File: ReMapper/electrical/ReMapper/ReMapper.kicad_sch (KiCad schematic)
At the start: 2 parts, among them U1 ESP32-S3-WROOM-1-N8R8, U2 SC0914_13_

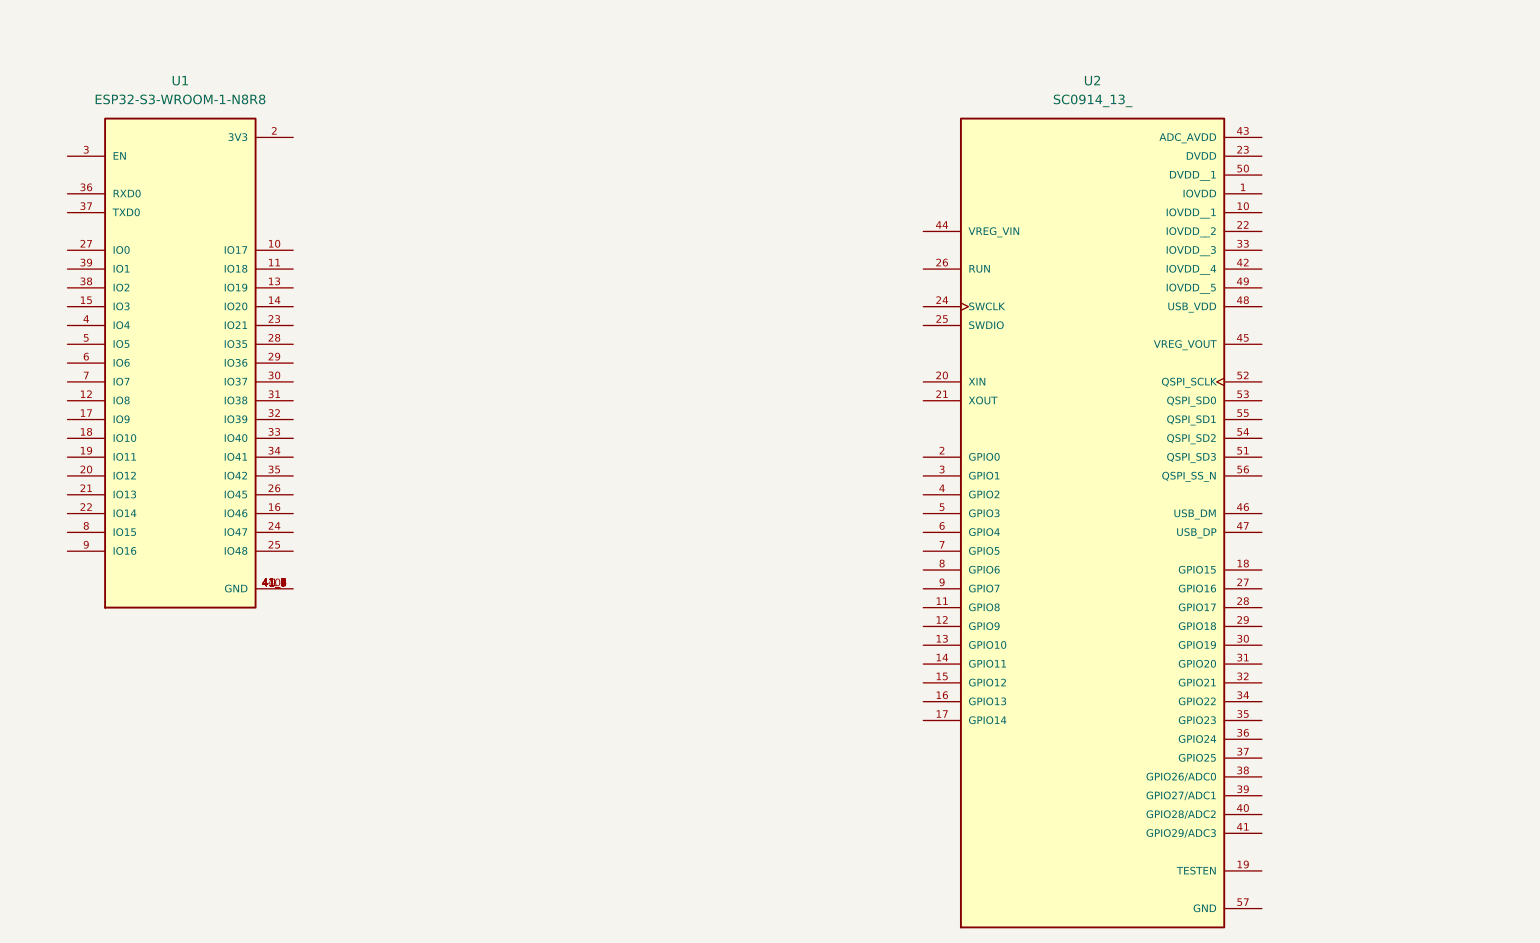
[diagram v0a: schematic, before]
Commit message: started working real schamtic
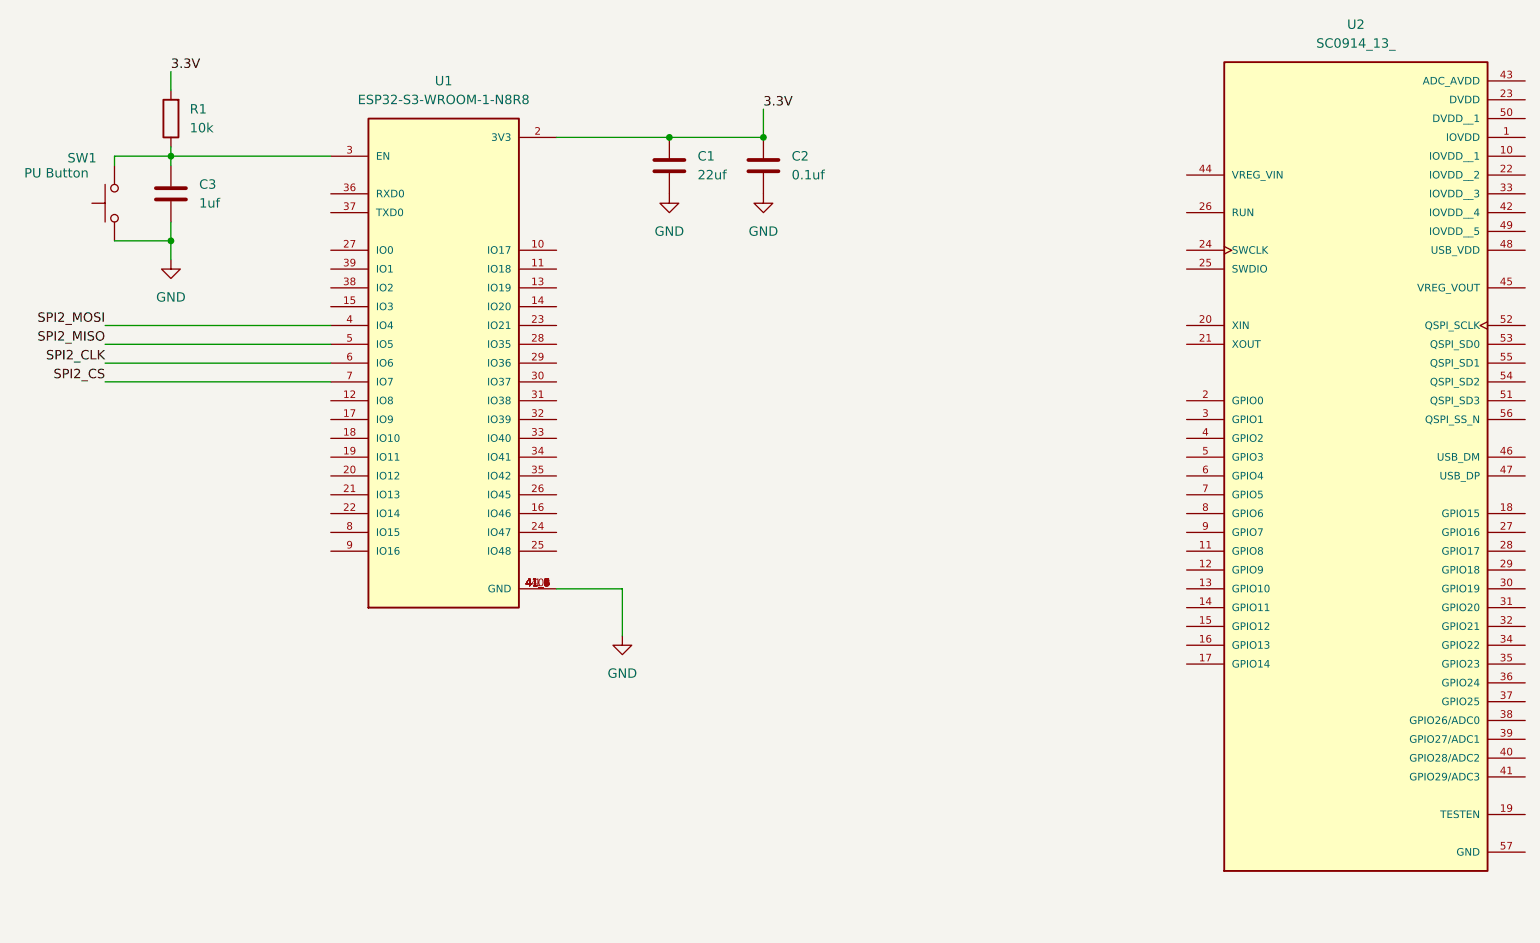
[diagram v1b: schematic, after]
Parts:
- added C1: 22uf, symbol Device:C
- added C2: 0.1uf, symbol Device:C
- added C3: 1uf, symbol Device:C
- added R1: 10k, symbol Device:R
- added SW1: PU Button, symbol Switch:SW_Push
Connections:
- net GND: now reaches U1.1 (GND), U1.40 (GND), U1.41_1 (GND), U1.41_2 (GND), U1.41_3 (GND), U1.41_4 (GND), U1.41_5 (GND), U1.41_6 (GND), U1.41_7 (GND), U1.41_8 (GND), U1.41_9 (GND)
- net GND: now also C1.2, C2.2, C3.2, SW1.1
- net 3.3V: now reaches U1.2 (3V3)
- net 3.3V: now also C1.1, C2.1, R1.2
- net at U1.3 (EN): now also C3.1, R1.1, SW1.2
- net SPI2_MOSI: now reaches U1.4 (IO4)
- net SPI2_MISO: now reaches U1.5 (IO5)
- net SPI2_CLK: now reaches U1.6 (IO6)
- net SPI2_CS: now reaches U1.7 (IO7)
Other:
- moved on the sheet: U1, U2

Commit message: more work on schematic
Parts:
- added C4: 2.2uf, symbol Device:C
- added C5: 100nf, symbol Device:C
- added C6, C7, C8: 47uF, symbol Device:C
- added D1: D_Schottky, symbol Device:D_Schottky
- added D2, D3, D4, D5: ESD, Diode_SMD:D_SOD-523, symbol Diode:ESD9B5.0ST5G
- added J1: QSPI_Debug, Connector_PinHeader_1.00mm:PinHeader_1x08_P1.00mm_Vertical, symbol Connector:Conn_01x08_Pin
- added J2: USB_IN, footprints:USBA_Female, symbol Connector:USB_A
- added J3: USB__IN_Debug, Connector_PinHeader_1.00mm:PinHeader_1x02_P1.00mm_Vertical, symbol Connector:Conn_01x02_Pin
- added J4: ESP_UART0, Connector_PinHeader_1.00mm:PinHeader_1x04_P1.00mm_Vertical, symbol Connector:Conn_01x04_Pin
- added J5: USB_OUT, footprints:USBA_Female, symbol Connector:USB_A
- added JP1: PFM Mode, Jumper:SolderJumper-2_P1.3mm_Open_Pad1.0x1.5mm, symbol Jumper:SolderJumper_2_Open
- added JP2, JP3: GND_SHIELD, Jumper:SolderJumper-2_P1.3mm_Open_Pad1.0x1.5mm, symbol Jumper:SolderJumper_2_Open
- added L1: 2.2uH, symbol Device:L
- added R2: 100k, symbol Device:R
- added U3: W25Q128JVE, Package_SON:WSON-8-1EP_8x6mm_P1.27mm_EP3.4x4.3mm, symbol Memory_Flash:W25Q128JVE
- added U4: RT6150B-33GQW, footprints:RT6150B-33GQW, symbol RT6150B-33GQW:RT6150B-33GQW
- U2: value SC0914_13_ -> RP2040
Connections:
- net 3.3V: now also C4.1, C5.1, C6.1, J1.7 (Pin_7), J4.1 (Pin_1), U3.8 (VCC), U4.1 (VOUT), U4.10 (FB)
- net GND: now also C4.2, C5.2, C6.2, C7.2, C8.2, D2.2 (A2), D3.1 (A1), D4.2 (A2), D5.1 (A1), J1.8 (Pin_8), J2.4 (GND), J4.4 (Pin_4), J5.4 (GND), JP2.2 (B), JP3.2 (B), R2.2, U3.4 (GND), U4.3 (GND), U4.9 (GND__1)
- net QSPI_CS_esp: now reaches U1.10 (IO17)
- net QSPI_CS_esp: now also J1.1 (Pin_1), U3.1 (~{CS})
- net USB_OUT_D+: now reaches U1.13 (IO19)
- net USB_OUT_D+: now also D2.1 (A1), J5.3 (D+)
- net USB_OUT_D-: now reaches U1.14 (IO20)
- net USB_OUT_D-: now also D3.2 (A2), J5.2 (D-)
- net QSPI_CLK_esp: now reaches U1.19 (IO11)
- net QSPI_CLK_esp: now also J1.2 (Pin_2), U3.6 (CLK)
- net QSPI_IO0_esp: now reaches U1.20 (IO12)
- net QSPI_IO0_esp: now also J1.3 (Pin_3), U3.5 (DI/IO_{0})
- net QSPI_IO1_esp: now reaches U1.21 (IO13)
- net QSPI_IO1_esp: now also J1.4 (Pin_4), U3.2 (DO/IO_{1})
- net QSPI_IO2_esp: now reaches U1.22 (IO14)
- net QSPI_IO2_esp: now also J1.5 (Pin_5), U3.3 (~{WP}/IO_{2})
- net QSPI_IO3_esp: now reaches U1.23 (IO21)
- net QSPI_IO3_esp: now also J1.6 (Pin_6), U3.7 (~{HOLD}/~{RESET}/IO_{3})
- net ESP_TXDO: now reaches U1.36 (RXD0)
- net ESP_TXDO: now also J4.2 (Pin_2)
- net ESP_RXDO: now reaches U1.37 (TXD0)
- net ESP_RXDO: now also J4.3 (Pin_3)
- new net: J5.5 (Shield), JP3.1 (A)
- new net: J2.5 (Shield), JP2.1 (A)
- new net: JP1.1 (A), R2.1, U4.7 (PS)
- new net: D1.2 (A), J2.1 (VBUS)
- new net: L1.1, U4.4 (LX1)
- new net: L1.2, U4.2 (LX2)
- new net USB_IN_D+: J2.3 (D+), J3.1 (Pin_1)
- new net USB_IN_D-: J2.2 (D-), J3.2 (Pin_2)
- new net USB_VIN: C7.1, C8.1, D1.1 (K), D4.1 (A1), D5.2 (A2), J5.1 (VBUS), JP1.2 (B), U4.5 (VIN), U4.6 (EN), U4.8 (VINA)
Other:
- note added: "DEBUG"
- note added: "ESP QSPI"
- note added: "ESP32-S3"
- note added: "Power"
- note added: "USB Buck Converter"
- note added: "USB IN"
- note added: "USB OUT"
- moved on the sheet: C3, R1, SW1, U2

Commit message: first draft schematic
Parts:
- added C10: 100nf, symbol Device:C
- added C11, C12: 15 pF, symbol Device:C
- added C9: 2.2uf, symbol Device:C
- added J6: USB_OUT_Debug, Connector_PinHeader_1.00mm:PinHeader_1x02_P1.00mm_Vertical, symbol Connector:Conn_01x02_Pin
- added JP4: RP_RUN, Jumper:SolderJumper-2_P1.3mm_Open_Pad1.0x1.5mm, symbol Jumper:SolderJumper_2_Open
- added JP5: RP_crystal, Jumper:SolderJumper-2_P1.3mm_Open_Pad1.0x1.5mm, symbol Jumper:SolderJumper_2_Open
- added R3: R, symbol Device:R
- added U5: W25Q128JVE, Package_SON:WSON-8-1EP_8x6mm_P1.27mm_EP3.4x4.3mm, symbol Memory_Flash:W25Q128JVE
- added Y1: 12MHZ, Crystal:Crystal_HC49-4H_Vertical, symbol Device:Crystal
- J3: value USB__IN_Debug -> USB_IN_Debug
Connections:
- net 3.3V: now also U2.1 (IOVDD), U2.10 (IOVDD__1), U2.22 (IOVDD__2), U2.33 (IOVDD__3), U2.42 (IOVDD__4), U2.43 (ADC_AVDD), U2.44 (VREG_VIN), U2.48 (USB_VDD), U2.49 (IOVDD__5), C10.1, C9.1, JP4.1 (A), U5.8 (VCC)
- net GND: now also U2.19 (TESTEN), U2.57 (GND), C10.2, C11.2, C12.2, C9.2, U5.4 (GND)
- net USB_OUT_D+: now also U2.46 (USB_DM), J6.1 (Pin_1)
- net USB_OUT_D-: now also U2.47 (USB_DP), J6.2 (Pin_2)
- net XIN_rp: now reaches U2.20 (XIN)
- net XIN_rp: now also C11.1, JP5.1 (A), Y1.1
- net XOUT_rp: now reaches U2.21 (XOUT)
- net XOUT_rp: now also JP5.2 (B), R3.1
- net at U2.23 (DVDD): now also U2.45 (VREG_VOUT), U2.50 (DVDD__1)
- net at U2.26 (RUN): now also JP4.2 (B)
- net QSPI_IO3_rp: now reaches U2.51 (QSPI_SD3)
- net QSPI_IO3_rp: now also U5.7 (~{HOLD}/~{RESET}/IO_{3})
- net QSPI_CLK_rp: now reaches U2.52 (QSPI_SCLK)
- net QSPI_CLK_rp: now also U5.6 (CLK)
- net QSPI_IO0_rp: now reaches U2.53 (QSPI_SD0)
- net QSPI_IO0_rp: now also U5.5 (DI/IO_{0})
- net QSPI_IO2_rp: now reaches U2.54 (QSPI_SD2)
- net QSPI_IO2_rp: now also U5.3 (~{WP}/IO_{2})
- net QSPI_IO1_rp: now reaches U2.55 (QSPI_SD1)
- net QSPI_IO1_rp: now also U5.2 (DO/IO_{1})
- net QSPI_CS_rp: now reaches U2.56 (QSPI_SS_N)
- net QSPI_CS_rp: now also U5.1 (~{CS})
- new net: C12.1, R3.2, Y1.2
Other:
- note added: "Raspberry Pi PICO"
- moved on the sheet: J3, J4, U2

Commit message: schematic first draft, onto layout
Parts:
- removed SW1: PU Button, symbol Switch:SW_Push
- added C13: 2.2uf, Capacitor_SMD:C_0603_1608Metric, symbol Device:C
- added D6: LED 33V, LED_SMD:LED_0603_1608Metric, symbol Device:LED
- added D7: LED USB VIN, LED_SMD:LED_0603_1608Metric, symbol Device:LED
- added D8, D9: LED RP5, LED_SMD:LED_0603_1608Metric, symbol Device:LED
- added R4: 1k, Resistor_SMD:R_0603_1608Metric, symbol Device:R
- added R5, R7, R8: 400, Resistor_SMD:R_0603_1608Metric, symbol Device:R
- added R6: 800, Resistor_SMD:R_0603_1608Metric, symbol Device:R
- added S1, S2: SKRPABE010, footprints:push_button_SKRPABE010, symbol push_button_SKRPABE010:SKRPABE010
- C1, C10, C11, C12, C2, C3, C4, C5, C6, C7, C8, C9: footprint (none) -> Capacitor_SMD:C_0603_1608Metric
- D1: footprint (none) -> Diode_SMD:D_SOD-123
- L1: footprint (none) -> Inductor_SMD:L_0603_1608Metric
- R1, R2: footprint (none) -> Resistor_SMD:R_0603_1608Metric
- R3: value R -> 1k; footprint (none) -> Resistor_SMD:R_0603_1608Metric
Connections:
- net 3.3V: now also C13.1, R5.1
- net GND: now also C13.2, D6.1 (K), D7.1 (K), D8.1 (K), D9.1 (K), S1.3, S1.4, S2.3, S2.4
- net QSPI_CS_rp: now also R4.2
- net SPI2_CLK: now also U2.29 (GPIO18)
- net SPI2_CS: now also U2.28 (GPIO17)
- net SPI2_MISO: now also U2.30 (GPIO19)
- net SPI2_MOSI: now also U2.27 (GPIO16)
- net USB_VIN: now also R6.1
- net GPIO5_rp: now reaches U2.7 (GPIO5)
- net GPIO5_rp: now also R7.1
- net at C3.1, R1.1, U1.3 (EN): now also S1.1, S1.2
- net IO8_esp: now reaches U1.12 (IO8)
- net IO8_esp: now also R8.1
- new net: D7.2 (A), R6.2
- new net: D6.2 (A), R5.2
- new net: R4.1, S2.1, S2.2
- new net: D9.2 (A), R8.2
- new net: D8.2 (A), R7.2
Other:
- note added: "INDICATORS"
- moved on the sheet: C10, C11, C12, C4, C5, C9, D1, JP4, JP5, R3, U2, U5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

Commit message: started layout
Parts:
- J5: footprint footprints:USBA_Female -> Connector_PinHeader_1.00mm:PinHeader_1x04_P1.00mm_Vertical
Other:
- moved on the sheet: D9, R8
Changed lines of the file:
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@@
 	(wire
 		(pts
-			(xy 382.27 44.45) (xy 382.27 45.72)
+			(xy 382.27 45.72) (xy 382.27 46.99)
 		)
 		(stroke
@@
 	(wire
 		(pts
-			(xy 382.27 24.13) (xy 382.27 27.94)
+			(xy 382.27 25.4) (xy 382.27 29.21)
 		)
 		(stroke
@@
 	(wire
 		(pts
-			(xy 382.27 35.56) (xy 382.27 36.83)
+			(xy 382.27 36.83) (xy 382.27 38.1)
 		)
 		(stroke
@@
 	)
 	(label "IO8_esp"
-		(at 382.27 24.13 180)
+		(at 382.27 25.4 180)
 		(effects
 			(font
@@
 			)
 		)
-		(property "Footprint" "footprints:USBA_Female"
+		(property "Footprint" "Connector_PinHeader_1.00mm:PinHeader_1x04_P1.00mm_Vertical"
 			(at 248.92 76.2 0)
 			(effects
@@
 	(symbol
 		(lib_id "Device:R")
-		(at 382.27 31.75 0)
+		(at 382.27 33.02 0)
 		(unit 1)
 		(exclude_from_sim no)
@@
 		(dnp no)
 		(property "Reference" "R8"
-			(at 384.81 30.4799 0)
+			(at 384.81 31.7499 0)
 			(effects
 				(font
@@
 		)
 		(property "Value" "400"
-			(at 384.81 33.0199 0)
+			(at 384.81 34.2899 0)
 			(effects
 				(font
@@
 		)
 		(property "Footprint" "Resistor_SMD:R_0603_1608Metric"
-			(at 380.492 31.75 90)
+			(at 380.492 33.02 90)
 			(effects
 				(font
@@
 		)
 		(property "Datasheet" "~"
-			(at 382.27 31.75 0)
+			(at 382.27 33.02 0)
 			(effects
 				(font
@@
 		)
 		(property "Description" "Resistor"
-			(at 382.27 31.75 0)
+			(at 382.27 33.02 0)
 			(effects
 				(font
@@
 	(symbol
 		(lib_id "power:GND")
-		(at 382.27 45.72 0)
+		(at 382.27 46.99 0)
 		(unit 1)
 		(exclude_from_sim no)
@@
 		(fields_autoplaced yes)
 		(property "Reference" "#PWR028"
-			(at 382.27 52.07 0)
+			(at 382.27 53.34 0)
 			(effects
 				(font
@@
 		)
 		(property "Value" "GND"
-			(at 382.27 50.8 0)
+			(at 382.27 52.07 0)
 			(effects
 				(font
@@
 		)
 		(property "Footprint" ""
-			(at 382.27 45.72 0)
+			(at 382.27 46.99 0)
 			(effects
 				(font
@@
 		)
 		(property "Datasheet" ""
-			(at 382.27 45.72 0)
+			(at 382.27 46.99 0)
 			(effects
 				(font
@@
 		)
 		(property "Description" "Power symbol creates a global label with name \"GND\" , ground"
-			(at 382.27 45.72 0)
+			(at 382.27 46.99 0)
 			(effects
 				(font
@@
 	(symbol
 		(lib_id "Device:LED")
-		(at 382.27 40.64 90)
+		(at 382.27 41.91 90)
 		(unit 1)
 		(exclude_from_sim no)
@@
 		(fields_autoplaced yes)
 		(property "Reference" "D9"
-			(at 386.08 40.9574 90)
+			(at 386.08 42.2274 90)
 			(effects
 				(font
@@
 		)
 		(property "Value" "LED RP5"
-			(at 386.08 43.4974 90)
+			(at 386.08 44.7674 90)
 			(effects
 				(font
@@
 		)
 		(property "Footprint" "LED_SMD:LED_0603_1608Metric"
-			(at 382.27 40.64 0)
+			(at 382.27 41.91 0)
 			(effects
 				(font
@@
 		)
 		(property "Datasheet" "~"
-			(at 382.27 40.64 0)
+			(at 382.27 41.91 0)
 			(effects
 				(font
@@
 		)
 		(property "Description" "Light emitting diode"
-			(at 382.27 40.64 0)
+			(at 382.27 41.91 0)
 			(effects
 				(font
@@
 		)
 		(property "Sim.Pins" "1=K 2=A"
-			(at 382.27 40.64 0)
+			(at 382.27 41.91 0)
 			(effects
 				(font
